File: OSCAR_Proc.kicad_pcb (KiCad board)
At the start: 2 copper layers, 91 x 88.6 mm, 87 parts, among them J1 Debug, J10 12V Audio, J11 ByPass, J2 USB, J3 SW1, J4 SW2, J5 MIDI_In, J6 12V, J7 SAI, J8 Volumes, J9 12V Audio, Q1 2N7002, SW1 Encoder0, SW2 Encoder1, SW3 Encoder2, SW4 Encoder3, SW5 BOOT, SW6 RESET, U1 STM32H743IIT6, U2 W25Q128JVS, U3 IS42S16320, U4 W25Q128JVS, U6 TFT, U7 H11L1, U8 AMS1117-3.3, Y1 25 Mhz

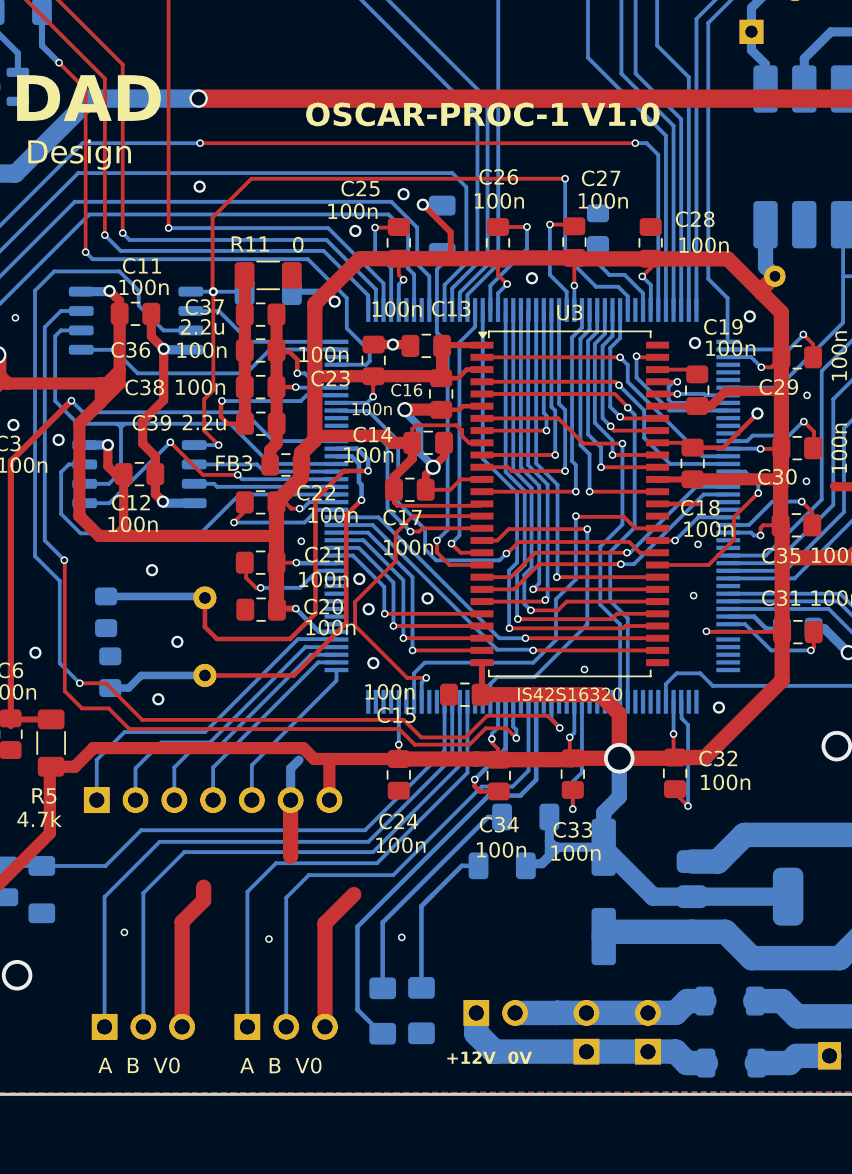
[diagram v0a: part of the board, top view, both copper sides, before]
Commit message: Reposition footswitch connectors and LEDs
- Moved footswitch connectors to support vertical placement
- Adjusted LED positions for better visibility
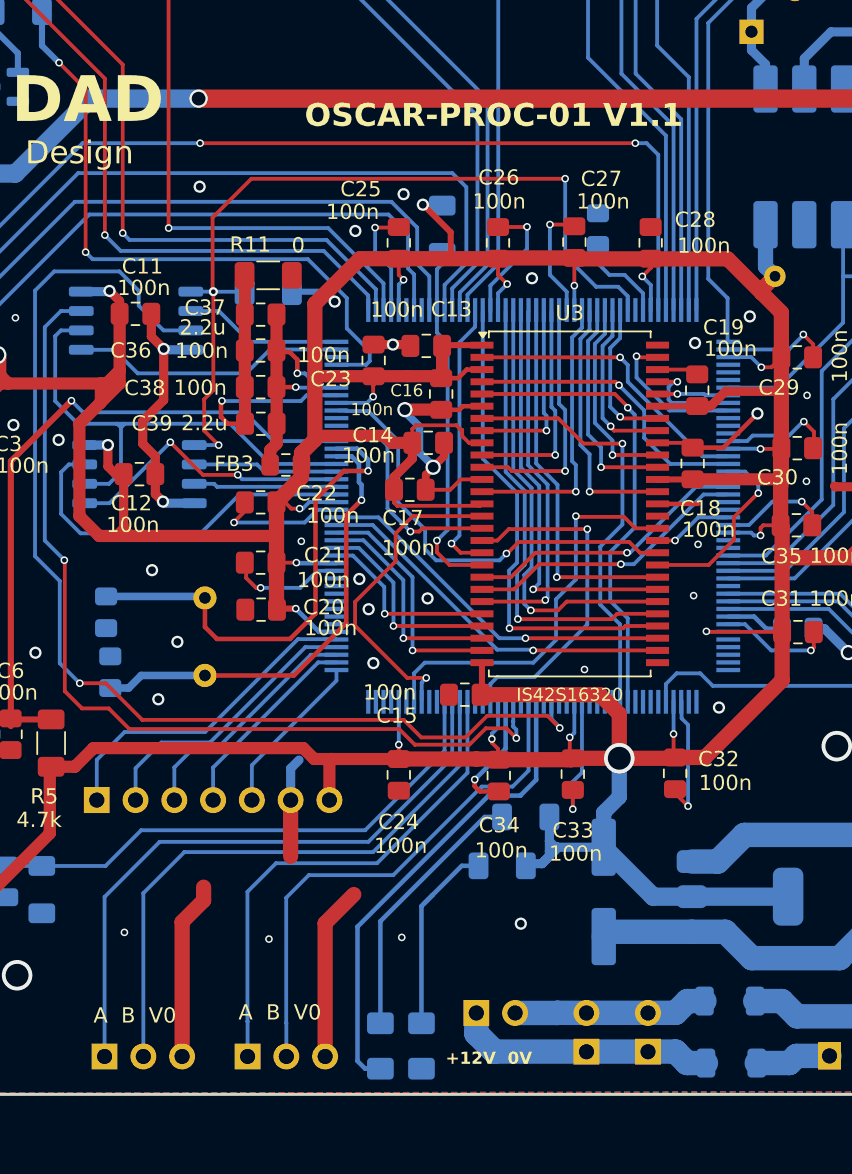
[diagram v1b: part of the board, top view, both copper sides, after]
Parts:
- moved D2 2.32 mm to (140.9, 108.8)
- moved D3 2.29 mm to (138.2, 108.8)
- moved J4 1.94 mm to (129.5, 109.5)
- moved J3 1.94 mm to (120.1, 109.5)
- renumbered REF** to H1, REF** to U2
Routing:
- net VSS: track 247.3 -> 251.2 mm, vias 62 -> 63
- net LED: track 28.5 -> 31.3 mm
- net Net-(D3-A): track 15.0 -> 17.5 mm
- net Net-(D2-A): track 11.0 -> 13.4 mm
- net SW2B: track 32.3 -> 34.2 mm
- net SW2A: track 31.1 -> 33.1 mm
- net SW1B: track 37.1 -> 39.1 mm
- net SW1A: track 38.7 -> 40.7 mm
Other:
- board text added: "OSCAR-PROC-01 V1.1"
- board text removed: "OSCAR-PROC-1 V1.0"
